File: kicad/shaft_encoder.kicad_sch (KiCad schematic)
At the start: 22 parts, among them U6 ISL3280ExHZ, U7 LS7184N-S, U8 ISL3280ExHZ

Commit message: Fixed up or explained all DRC violations.
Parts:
- renumbered R16 to R19, R17 to R20, R18 to R21, R19 to R22, R20 to R23, R21 to R24, R22 to R25
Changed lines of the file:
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@@
 		(dnp no)
 		(fields_autoplaced yes)
-		(property "Reference" "R20"
+		(property "Reference" "R23"
 			(at 167.64 91.4399 0)
 			(effects
@@
 			(project "tv_slider"
 				(path "/914c4b67-a7a4-47f3-8515-668040fd3f8c/5fc52a5d-8056-4e66-b25c-e5367f161659"
-					(reference "R20")
+					(reference "R23")
 					(unit 1)
 				)
@@
 		(dnp no)
 		(fields_autoplaced yes)
-		(property "Reference" "#PWR084"
+		(property "Reference" "#PWR085"
 			(at 137.16 119.38 0)
 			(effects
@@
 			(project "tv_slider"
 				(path "/914c4b67-a7a4-47f3-8515-668040fd3f8c/5fc52a5d-8056-4e66-b25c-e5367f161659"
-					(reference "#PWR084")
+					(reference "#PWR085")
 					(unit 1)
 				)
@@
 		(dnp no)
 		(fields_autoplaced yes)
-		(property "Reference" "#PWR094"
+		(property "Reference" "#PWR095"
 			(at 157.48 179.07 0)
 			(effects
@@
 			(project "tv_slider"
 				(path "/914c4b67-a7a4-47f3-8515-668040fd3f8c/5fc52a5d-8056-4e66-b25c-e5367f161659"
-					(reference "#PWR094")
+					(reference "#PWR095")
 					(unit 1)
 				)
@@
 		(dnp no)
 		(fields_autoplaced yes)
-		(property "Reference" "R22"
+		(property "Reference" "R25"
 			(at 88.9 104.14 90)
 			(effects
@@
 			(project "tv_slider"
 				(path "/914c4b67-a7a4-47f3-8515-668040fd3f8c/5fc52a5d-8056-4e66-b25c-e5367f161659"
-					(reference "R22")
+					(reference "R25")
 					(unit 1)
 				)
@@
 		(dnp no)
 		(fields_autoplaced yes)
-		(property "Reference" "#PWR076"
+		(property "Reference" "#PWR077"
 			(at 208.28 73.66 0)
 			(effects
@@
 			(project ""
 				(path "/914c4b67-a7a4-47f3-8515-668040fd3f8c/5fc52a5d-8056-4e66-b25c-e5367f161659"
-					(reference "#PWR076")
+					(reference "#PWR077")
 					(unit 1)
 				)
@@
 		(dnp no)
 		(fields_autoplaced yes)
-		(property "Reference" "R16"
+		(property "Reference" "R19"
 			(at 88.9 50.8 90)
 			(effects
@@
 			(project "tv_slider"
 				(path "/914c4b67-a7a4-47f3-8515-668040fd3f8c/5fc52a5d-8056-4e66-b25c-e5367f161659"
-					(reference "R16")
+					(reference "R19")
 					(unit 1)
 				)
@@
 		(dnp no)
 		(fields_autoplaced yes)
-		(property "Reference" "R21"
+		(property "Reference" "R24"
 			(at 115.57 100.3299 0)
 			(effects
@@
 			(project "tv_slider"
 				(path "/914c4b67-a7a4-47f3-8515-668040fd3f8c/5fc52a5d-8056-4e66-b25c-e5367f161659"
-					(reference "R21")
+					(reference "R24")
 					(unit 1)
 				)
@@
 		(dnp no)
 		(fields_autoplaced yes)
-		(property "Reference" "R18"
+		(property "Reference" "R21"
 			(at 88.9 68.58 90)
 			(effects
@@
 			(project "tv_slider"
 				(path "/914c4b67-a7a4-47f3-8515-668040fd3f8c/5fc52a5d-8056-4e66-b25c-e5367f161659"
-					(reference "R18")
+					(reference "R21")
 					(unit 1)
 				)
@@
 		(dnp no)
 		(fields_autoplaced yes)
-		(property "Reference" "#PWR087"
+		(property "Reference" "#PWR088"
 			(at 85.09 148.59 0)
 			(effects
@@
 			(project "tv_slider"
 				(path "/914c4b67-a7a4-47f3-8515-668040fd3f8c/5fc52a5d-8056-4e66-b25c-e5367f161659"
-					(reference "#PWR087")
+					(reference "#PWR088")
 					(unit 1)
 				)
@@
 		(dnp no)
 		(fields_autoplaced yes)
-		(property "Reference" "#PWR080"
+		(property "Reference" "#PWR081"
 			(at 165.1 105.41 0)
 			(effects
@@
 			(project "tv_slider"
 				(path "/914c4b67-a7a4-47f3-8515-668040fd3f8c/5fc52a5d-8056-4e66-b25c-e5367f161659"
-					(reference "#PWR080")
+					(reference "#PWR081")
 					(unit 1)
 				)
@@
 		(dnp no)
 		(fields_autoplaced yes)
-		(property "Reference" "#PWR086"
+		(property "Reference" "#PWR087"
 			(at 73.66 148.59 0)
 			(effects
@@
 			(project "tv_slider"
 				(path "/914c4b67-a7a4-47f3-8515-668040fd3f8c/5fc52a5d-8056-4e66-b25c-e5367f161659"
-					(reference "#PWR086")
+					(reference "#PWR087")
 					(unit 1)
 				)
@@
 		(dnp no)
 		(fields_autoplaced yes)
-		(property "Reference" "#PWR091"
+		(property "Reference" "#PWR092"
 			(at 157.48 166.37 0)
 			(effects
@@
 			(project "tv_slider"
 				(path "/914c4b67-a7a4-47f3-8515-668040fd3f8c/5fc52a5d-8056-4e66-b25c-e5367f161659"
-					(reference "#PWR091")
+					(reference "#PWR092")
 					(unit 1)
 				)
@@
 		(dnp no)
 		(fields_autoplaced yes)
-		(property "Reference" "#PWR093"
+		(property "Reference" "#PWR094"
 			(at 142.24 179.07 0)
 			(effects
@@
 			(project "tv_slider"
 				(path "/914c4b67-a7a4-47f3-8515-668040fd3f8c/5fc52a5d-8056-4e66-b25c-e5367f161659"
-					(reference "#PWR093")
+					(reference "#PWR094")
 					(unit 1)
 				)
@@
 		(dnp no)
 		(fields_autoplaced yes)
-		(property "Reference" "#PWR085"
+		(property "Reference" "#PWR086"
 			(at 133.35 135.89 0)
 			(effects
@@
 			(project ""
 				(path "/914c4b67-a7a4-47f3-8515-668040fd3f8c/5fc52a5d-8056-4e66-b25c-e5367f161659"
-					(reference "#PWR085")
+					(reference "#PWR086")
 					(unit 1)
 				)
@@
 		(dnp no)
 		(fields_autoplaced yes)
-		(property "Reference" "#PWR092"
+		(property "Reference" "#PWR093"
 			(at 127 179.07 0)
 			(effects
@@
 			(project "tv_slider"
 				(path "/914c4b67-a7a4-47f3-8515-668040fd3f8c/5fc52a5d-8056-4e66-b25c-e5367f161659"
-					(reference "#PWR092")
+					(reference "#PWR093")
 					(unit 1)
 				)
@@
 		(dnp no)
 		(fields_autoplaced yes)
-		(property "Reference" "R17"
+		(property "Reference" "R20"
 			(at 115.57 64.7699 0)
 			(effects
@@
 			(project ""
 				(path "/914c4b67-a7a4-47f3-8515-668040fd3f8c/5fc52a5d-8056-4e66-b25c-e5367f161659"
-					(reference "R17")
+					(reference "R20")
 					(unit 1)
 				)
@@
 		(dnp no)
 		(fields_autoplaced yes)
-		(property "Reference" "#PWR082"
+		(property "Reference" "#PWR083"
 			(at 208.28 105.41 0)
 			(effects
@@
 			(project ""
 				(path "/914c4b67-a7a4-47f3-8515-668040fd3f8c/5fc52a5d-8056-4e66-b25c-e5367f161659"
-					(reference "#PWR082")
+					(reference "#PWR083")
 					(unit 1)
 				)
@@
 		(dnp no)
 		(fields_autoplaced yes)
-		(property "Reference" "#PWR081"
+		(property "Reference" "#PWR082"
 			(at 172.72 105.41 0)
 			(effects
@@
 			(project ""
 				(path "/914c4b67-a7a4-47f3-8515-668040fd3f8c/5fc52a5d-8056-4e66-b25c-e5367f161659"
-					(reference "#PWR081")
+					(reference "#PWR082")
 					(unit 1)
 				)
@@
 		(dnp no)
 		(fields_autoplaced yes)
-		(property "Reference" "#PWR088"
+		(property "Reference" "#PWR089"
 			(at 96.52 148.59 0)
 			(effects
@@
 			(project "tv_slider"
 				(path "/914c4b67-a7a4-47f3-8515-668040fd3f8c/5fc52a5d-8056-4e66-b25c-e5367f161659"
-					(reference "#PWR088")
+					(reference "#PWR089")
 					(unit 1)
 				)
@@
 		(dnp no)
 		(fields_autoplaced yes)
-		(property "Reference" "#PWR075"
+		(property "Reference" "#PWR076"
 			(at 137.16 58.42 0)
 			(effects
@@
 			(project "tv_slider"
 				(path "/914c4b67-a7a4-47f3-8515-668040fd3f8c/5fc52a5d-8056-4e66-b25c-e5367f161659"
-					(reference "#PWR075")
+					(reference "#PWR076")
 					(unit 1)
 				)
@@
 		(dnp no)
 		(fields_autoplaced yes)
-		(property "Reference" "#PWR079"
+		(property "Reference" "#PWR080"
 			(at 137.16 93.98 0)
 			(effects
@@
 			(project "tv_slider"
 				(path "/914c4b67-a7a4-47f3-8515-668040fd3f8c/5fc52a5d-8056-4e66-b25c-e5367f161659"
-					(reference "#PWR079")
+					(reference "#PWR080")
 					(unit 1)
 				)
@@
 		(dnp no)
 		(fields_autoplaced yes)
-		(property "Reference" "R19"
+		(property "Reference" "R22"
 			(at 88.9 86.36 90)
 			(effects
@@
 			(project "tv_slider"
 				(path "/914c4b67-a7a4-47f3-8515-668040fd3f8c/5fc52a5d-8056-4e66-b25c-e5367f161659"
-					(reference "R19")
+					(reference "R22")
 					(unit 1)
 				)
@@
 		(dnp no)
 		(fields_autoplaced yes)
-		(property "Reference" "#PWR077"
+		(property "Reference" "#PWR078"
 			(at 80.01 83.82 0)
 			(effects
@@
 			(project "tv_slider"
 				(path "/914c4b67-a7a4-47f3-8515-668040fd3f8c/5fc52a5d-8056-4e66-b25c-e5367f161659"
-					(reference "#PWR077")
+					(reference "#PWR078")
 					(unit 1)
 				)
@@
 		(dnp no)
 		(fields_autoplaced yes)
-		(property "Reference" "#PWR090"
+		(property "Reference" "#PWR091"
 			(at 142.24 166.37 0)
 			(effects
@@
 			(project "tv_slider"
 				(path "/914c4b67-a7a4-47f3-8515-668040fd3f8c/5fc52a5d-8056-4e66-b25c-e5367f161659"
-					(reference "#PWR090")
+					(reference "#PWR091")
 					(unit 1)
 				)
@@
 		(dnp no)
 		(fields_autoplaced yes)
-		(property "Reference" "#PWR089"
+		(property "Reference" "#PWR090"
 			(at 127 166.37 0)
 			(effects
@@
 			(project "tv_slider"
 				(path "/914c4b67-a7a4-47f3-8515-668040fd3f8c/5fc52a5d-8056-4e66-b25c-e5367f161659"
-					(reference "#PWR089")
+					(reference "#PWR090")
 					(unit 1)
 				)
@@
 		(dnp no)
 		(fields_autoplaced yes)
-		(property "Reference" "#PWR078"
+		(property "Reference" "#PWR079"
 			(at 137.16 83.82 0)
 			(effects
@@
 			(project "tv_slider"
 				(path "/914c4b67-a7a4-47f3-8515-668040fd3f8c/5fc52a5d-8056-4e66-b25c-e5367f161659"
-					(reference "#PWR078")
+					(reference "#PWR079")
 					(unit 1)
 				)
@@
 		(dnp no)
 		(fields_autoplaced yes)
-		(property "Reference" "#PWR083"
+		(property "Reference" "#PWR084"
 			(at 80.01 119.38 0)
 			(effects
@@
 			(project "tv_slider"
 				(path "/914c4b67-a7a4-47f3-8515-668040fd3f8c/5fc52a5d-8056-4e66-b25c-e5367f161659"
-					(reference "#PWR083")
+					(reference "#PWR084")
 					(unit 1)
 				)

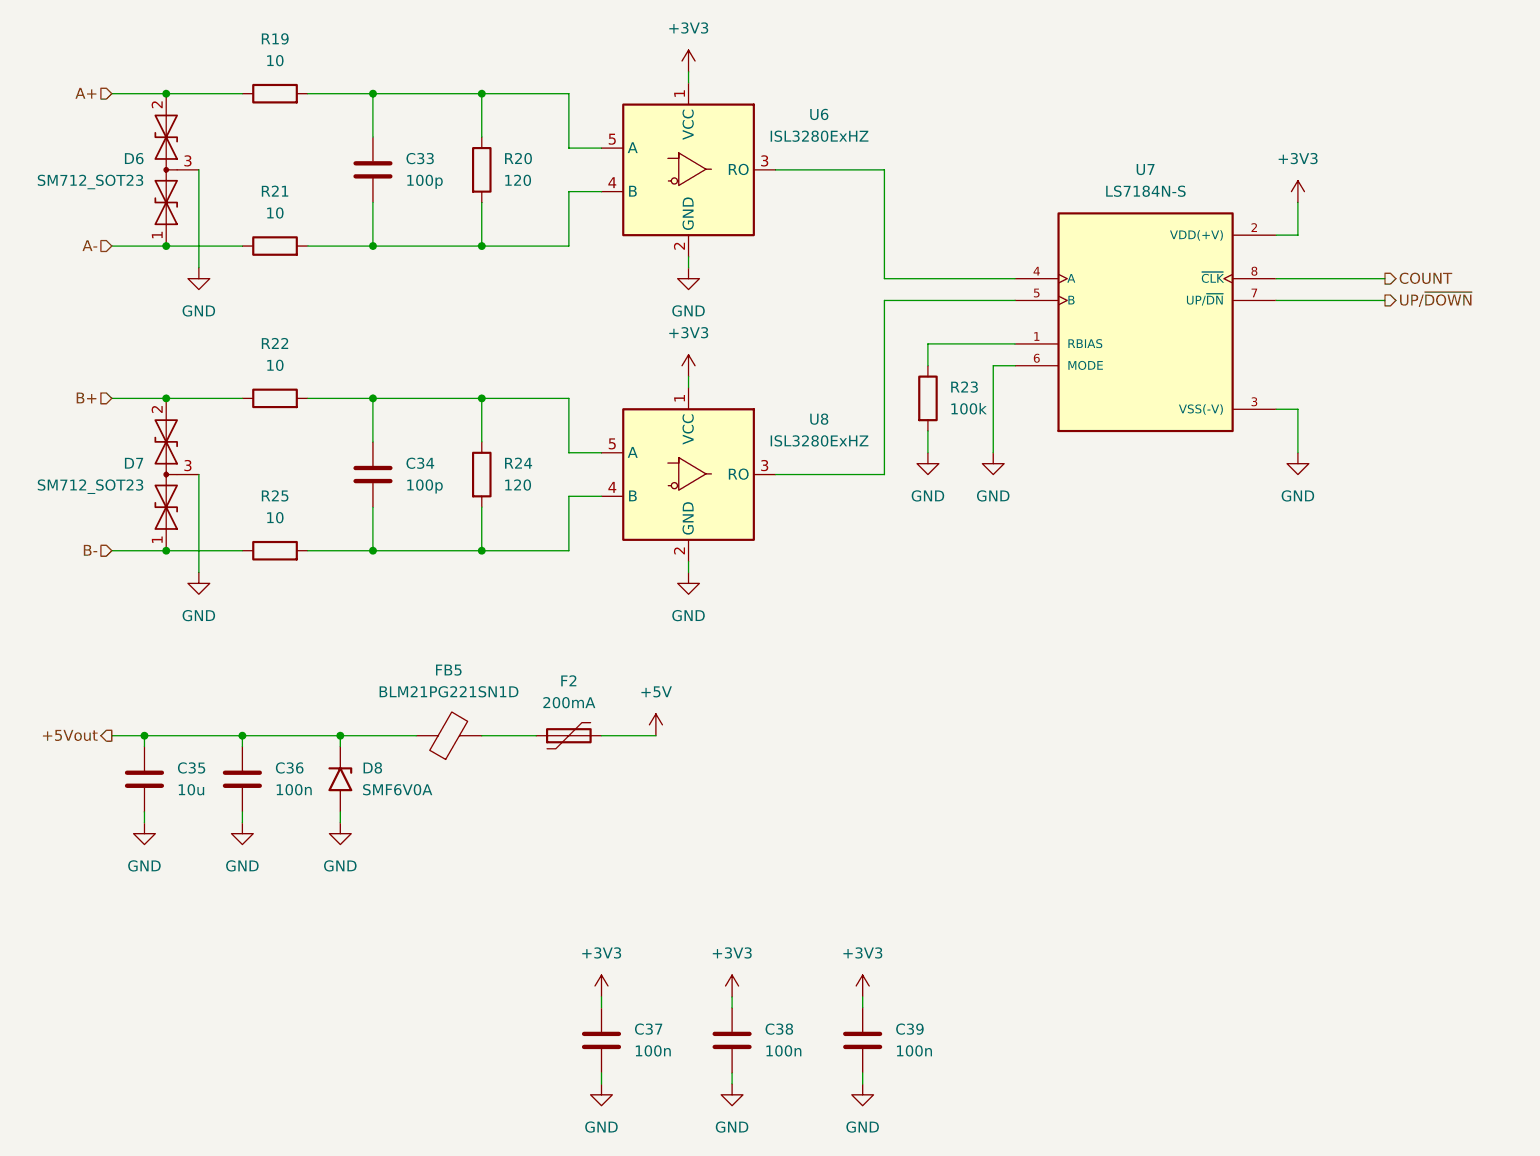
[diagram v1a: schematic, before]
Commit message: Supplying the ESP32-C6-DEVKIT with 5V and using its 3V3 output to supply the boards logic. Removed the 3V3 switch mode power supply on the board.
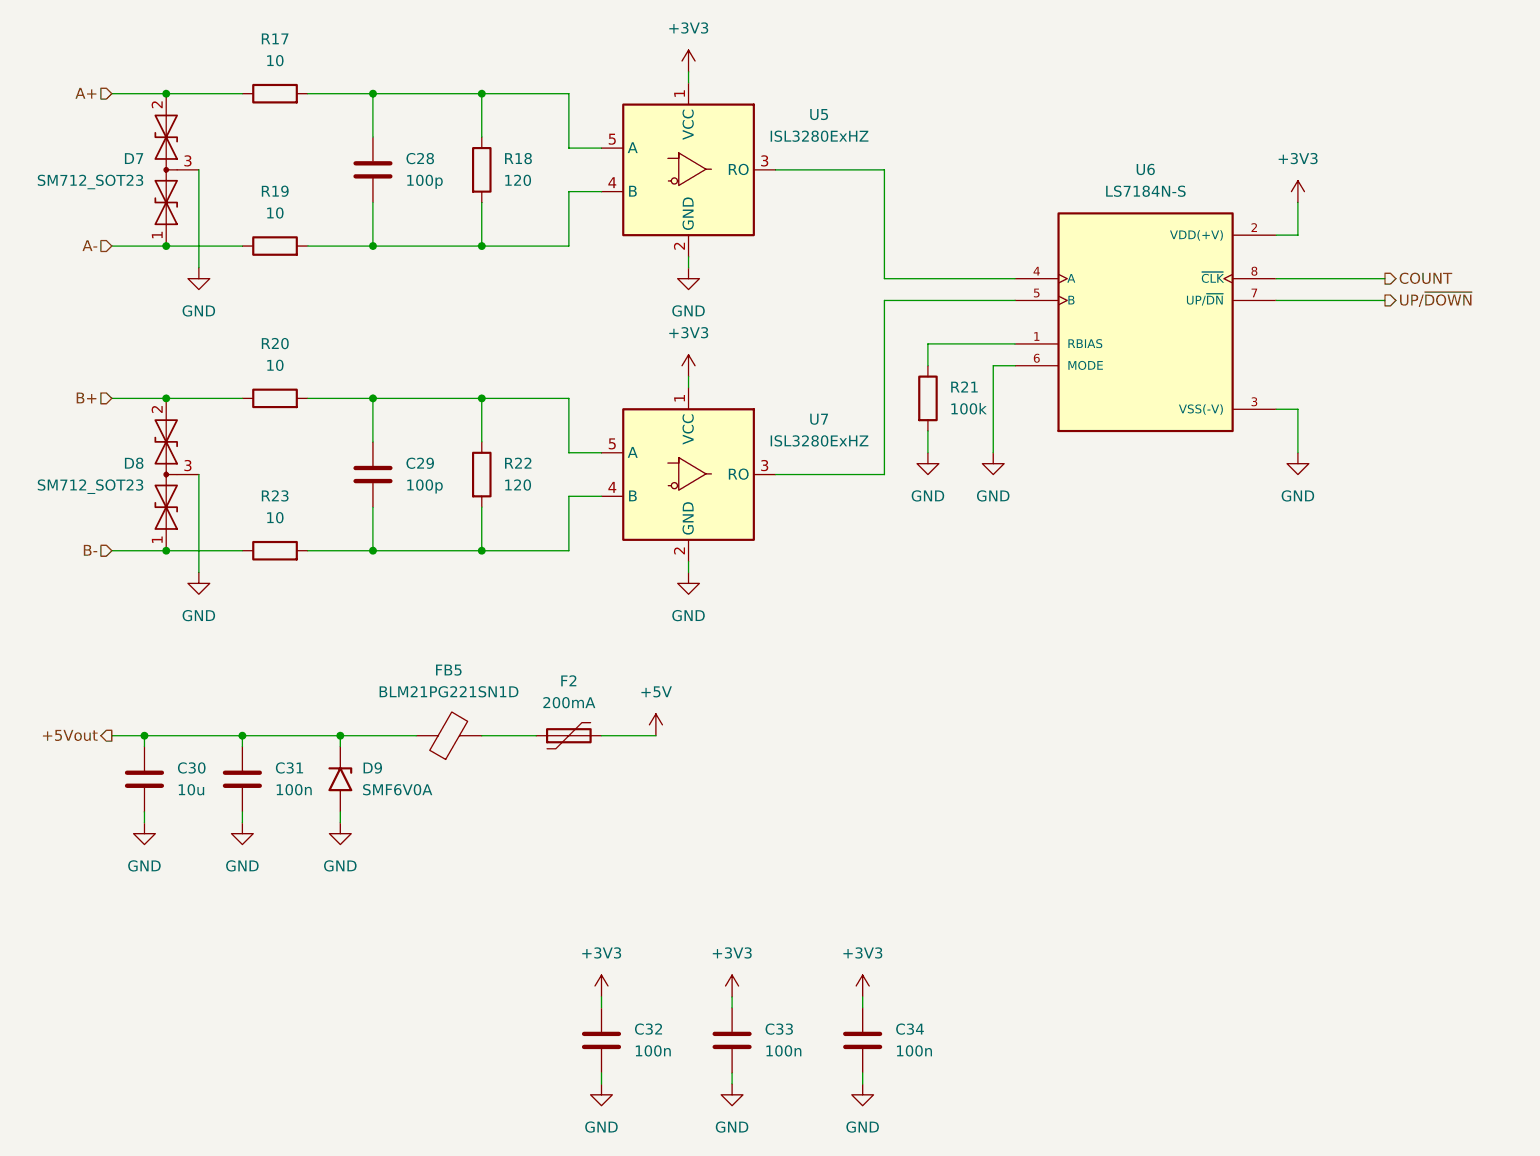
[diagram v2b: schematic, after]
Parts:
- renumbered C33 to C28, C34 to C29, C35 to C30, C36 to C31, C37 to C32, C38 to C33, C39 to C34, D6 to D7, D7 to D8, D8 to D9, R19 to R17, R20 to R18, R21 to R19, R22 to R20, R23 to R21, R24 to R22, R25 to R23, U6 to U5, U7 to U6, U8 to U7

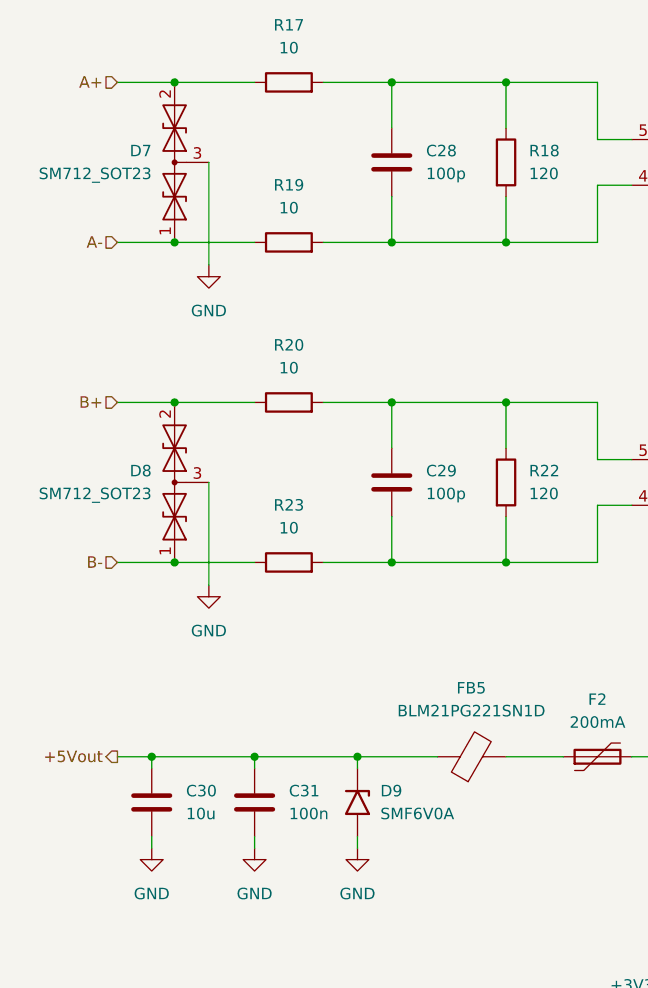
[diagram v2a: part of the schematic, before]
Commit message: Updated to use more of JCLPCB's basic components. Added extra field "FT Rotation Offset" to get the correct orientation for placement at JCLPCB.
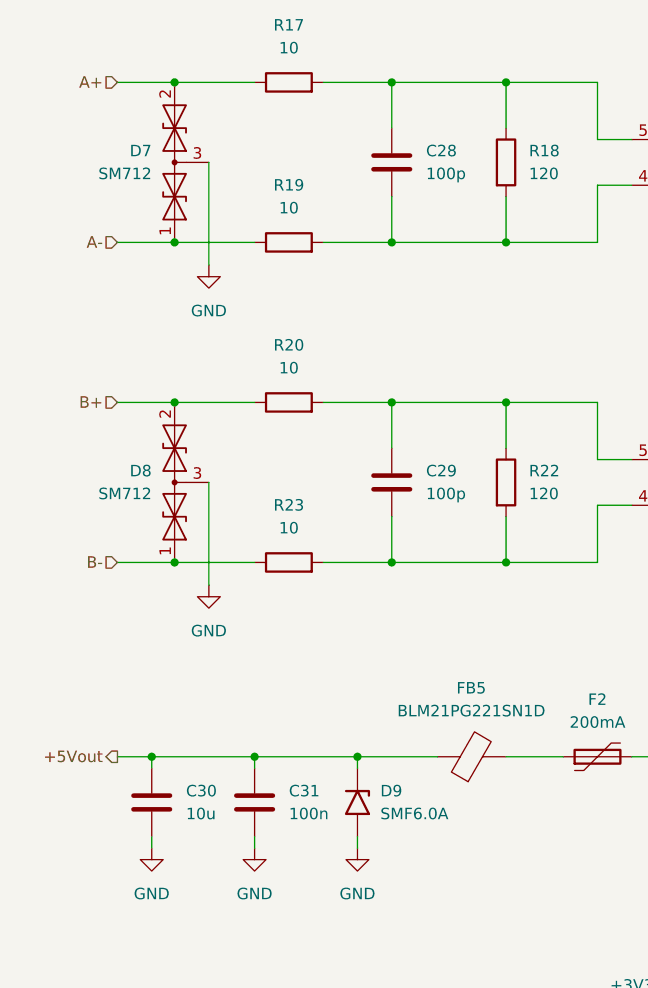
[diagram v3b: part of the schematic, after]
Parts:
- C28, C29: Dielectric C0G, NP0 -> (none); LCSC (none) -> C14858; MF Murata -> Samsung; MP GRM1885C1H101JA01D -> CL10C101JB8NNNC; SupplierPN 490-1427-1-ND -> 1276-1008-1-ND
- C30: Dielectric X5R -> (none); LCSC (none) -> C440198
- C31, C32, C33, C34: Dielectric X7R -> (none); LCSC (none) -> C14663; MF Murata -> Yageo; MP GRM188R72A104KA35D -> CC0603KRX7R9BB104; SupplierPN 490-3285-1-ND -> 311-1344-1-ND; Voltage 100V -> 50V
- D7, D8: value SM712_SOT23 -> SM712; LCSC (none) -> C7420375; MF SMC Diode Solutions -> Hong Jiacheng; SupplierPN 1655-SM712CT-ND -> 5399-SM712CT-ND
- D9: value SMF6V0A -> SMF6.0A; footprint Diode_SMD:D_SMF -> Diode_SMD:D_SOD-123F; LCSC (none) -> C19077499; MF Vishay -> Hong Jiacheng; MP SMF6V0A-E3-08 -> SMF6.0A; SupplierPN SMF6V0A-E3-08CT-ND -> 5399-SMF6.0ACT-ND
- F2: LCSC (none) -> C207035; Voltage 60V -> (none)
- FB5: LCSC (none) -> C1015; MF Murata -> Sunlord; MP BLM21PG221SN1D -> GZ2012D101TF
- R17, R19, R20, R23: LCSC (none) -> C22859; MF Yageo -> Uni Royal; MP RC0603FR-0710RL -> 0603WAF100JT5E
- R18, R22: LCSC (none) -> C22787; MF Yageo -> Uni Royal; MP RC0603FR-07120RL -> 0603WAF1200T5E
- R21: LCSC (none) -> C25803; MF Yageo -> Uni Royal; MP RC0603FR-07100KL -> 0603WAF1003T5E
- U5, U7: LCSC (none) -> C3227945; MP ISL3280EIHZ-T -> ISL3280EFHZ-T; SupplierPN ISL3280EIHZ-TCT-ND -> 20-ISL3280EFHZ-TCT-ND
- U6: FT Rotation Offset (none) -> 90; LCSC (none) -> C3234980
